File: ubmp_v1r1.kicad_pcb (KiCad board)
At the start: 2 copper layers, 34.5 x 14 mm, 34 parts, among them J1 Conn_02x05_Counter_Clockwise, J2 USB_A, U1 STM32F103CBUx, U2 MIC5245-3.3, Y1 PRQC8.00CR1010V00L

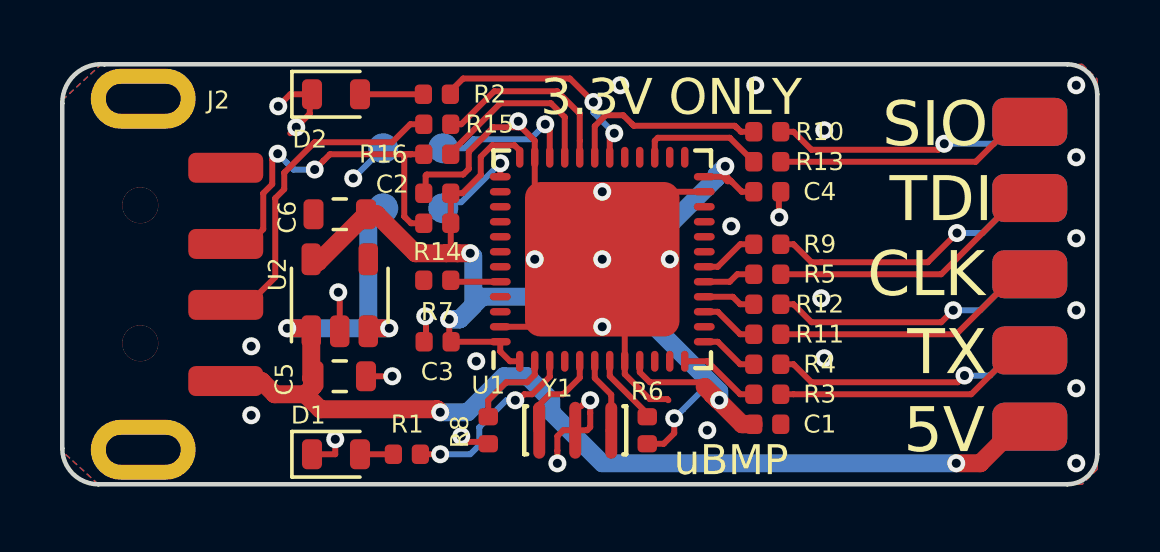
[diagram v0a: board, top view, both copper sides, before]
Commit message: Now more compatible with STLink-v2
Changes:
* Fixed 0603 cap spacing
* Added fuse to 5V line
* Connected unused signals from STLink schematic
* Connected BOOT1 to GND
* Removed yellow LED
* Updated width of USB connector pads for easier soldering
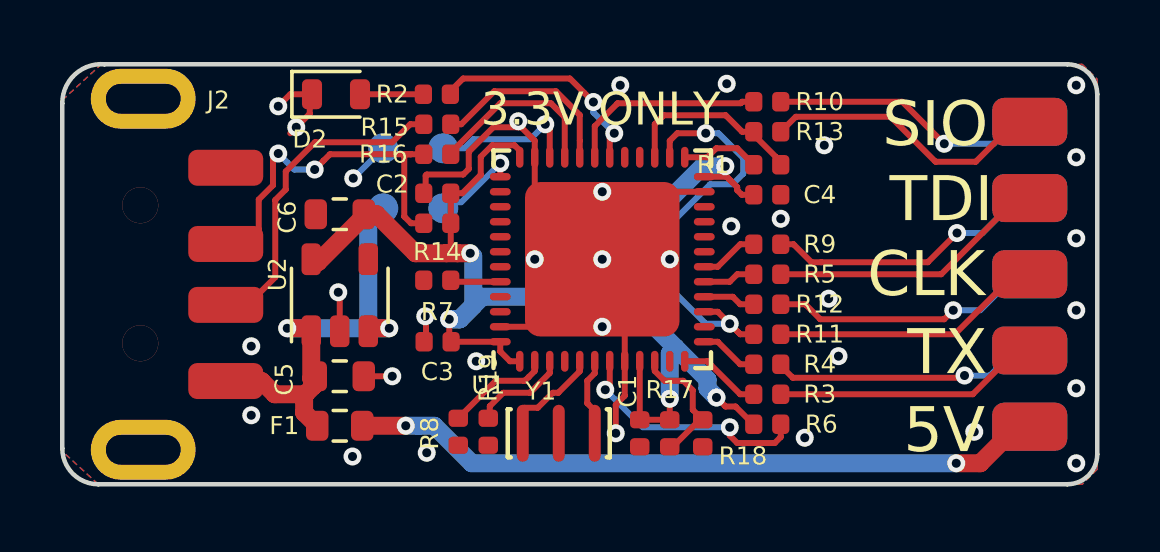
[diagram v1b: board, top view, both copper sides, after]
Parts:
- removed D1: YELLOW, ubmp:D_0603_1608Metric_Rounded
- added F1: MF-FSMF050X-2, ubmp:R_0603_1608Metric_Rounded, F.Cu at (94.2, 111.0)
- added R17: 1.5k, ubmp:R_0402_1005Metric_Rounded, F.Cu at (105.2, 111.3)
- added R18: 1.5k, ubmp:R_0402_1005Metric_Rounded, F.Cu at (106.3, 111.3)
- added R19: 1.5k, ubmp:R_0402_1005Metric_Rounded, F.Cu at (99.2, 111.2)
- R1: value 470 -> 100
- moved R1 15.4 mm to (108.5, 102.3), turned to 0 degrees
- moved C1 4.26 mm to (104.2, 111.3), turned to 270 degrees
- moved R6 4.00 mm to (108.5, 111.0), turned to 180 degrees
- moved R8 1.00 mm to (98.2, 111.2)
- moved R10 1.00 mm to (108.5, 100.2)
- moved R13 1.00 mm to (108.5, 101.2)
- moved Y1 0.56 mm to (101.5, 111.3)
- moved C4 0.10 mm to (108.5, 103.3)
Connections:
- J1 pad 1: +5V -> Net-(F1-Pad1)
- R1 pad 1: /LED_UART -> /STLINK_SWDIO_IN
- R1 pad 2: Net-(D1-Pad2) -> /BMP_SWDIO_TMS
- U1 pad 10: Net-(U1-Pad10) -> /STLINK_AIN_1
- U1 pad 20: Net-(U1-Pad20) -> GND
- U1 pad 25: Net-(U1-Pad25) -> /STLINK_SWDIO_IN
- U1 pad 26: Net-(U1-Pad26) -> /BMP_SWCLK_TCK
- U1 pad 3: /LED_UART -> /STM_ID2
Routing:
- net +5V: track 42.0 -> 16.4 mm, vias 4 -> 2
- net Net-(F1-Pad1): track 0.00 -> 23.3 mm, vias 0 -> 2
- net /BMP_SWCLK_TCK: track 2.02 -> 14.8 mm, vias 0 -> 2
- net /LED_UART: track 6.31 -> 0.00 mm, vias 2 -> 0
- net GND: track 39.3 -> 33.3 mm
- net /NRST: track 2.35 -> 8.27 mm, vias 0 -> 2
- net /STLINK_AIN_1: track 0.00 -> 4.45 mm
- net /STM_ID2: track 0.00 -> 3.35 mm
- net /STLINK_SWDIO_IN: track 0.00 -> 2.65 mm
- net /BMP_SWDIO_TMS: track 4.29 -> 6.22 mm
- net +3V3: track 46.6 -> 45.5 mm
- net Net-(D1-Pad2): track 1.11 -> 0.00 mm
- net /BMP_SWDIO_TMSo: track 8.91 -> 9.68 mm
- net /STM_ID: track 2.96 -> 3.57 mm
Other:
- board text removed: "uBMP"

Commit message: Updated PCB version number, generated new schematic
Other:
- board text added: "µBMP v1.1"
- board text removed: "µBMP v1.0"
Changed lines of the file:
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@@
     (effects (font (size 1.5 1.5) (thickness 0.3)) (justify mirror))
   )
-  (gr_text "µBMP v1.0" (at 101.8 108.6) (layer B.SilkS)
+  (gr_text "µBMP v1.1" (at 101.8 108.6) (layer B.SilkS)
     (effects (font (size 2 2) (thickness 0.4)) (justify mirror))
   )

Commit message: Updated reset circuit and updated silkscreen layout
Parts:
- removed R6: 1.5k, ubmp:R_0402_1005Metric_Rounded
- added C7: 100n, ubmp:C_0402_1005Metric_Rounded, F.Cu at (108.5, 111.0)
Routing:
- net +3V3: track 45.5 -> 41.2 mm, vias 5 -> 4
- net /NRST: track 8.27 -> 6.69 mm

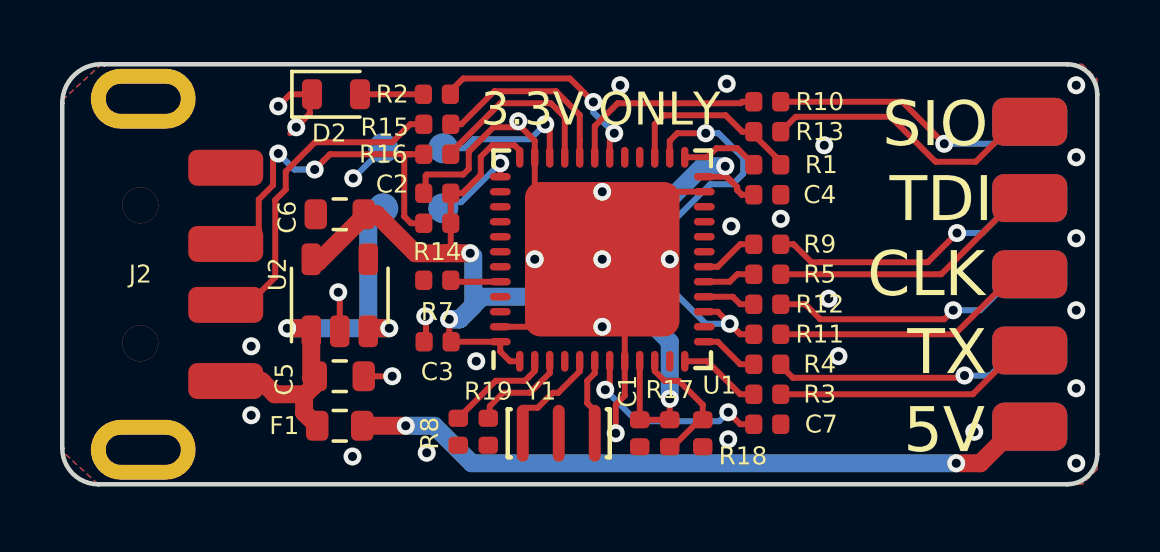
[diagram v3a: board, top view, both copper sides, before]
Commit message: Reverted STlink compatibility changes and updated a lot of footprints
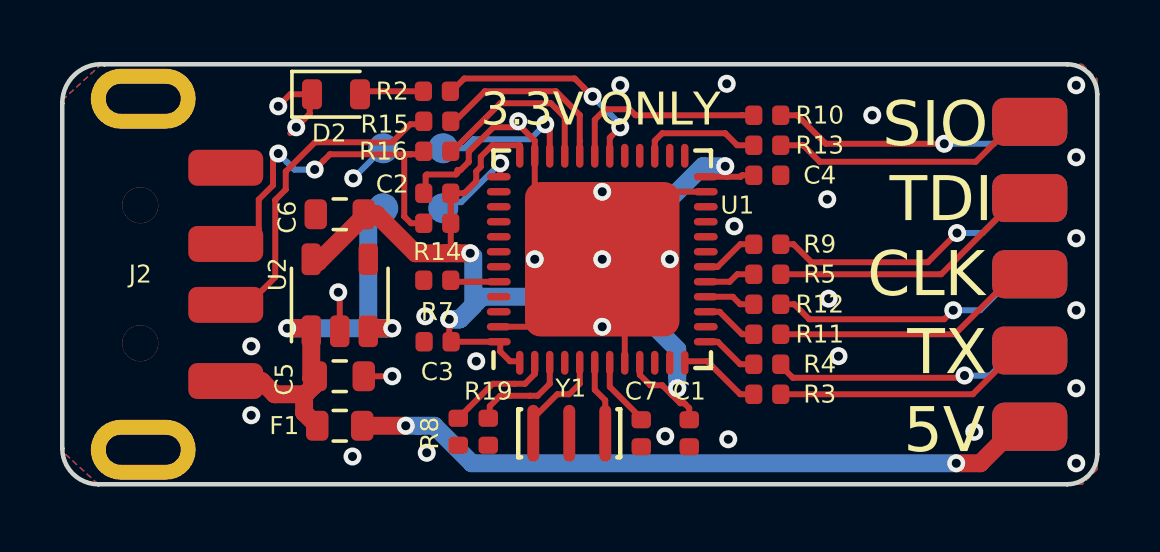
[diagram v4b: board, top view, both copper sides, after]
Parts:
- removed R1: 100, ubmp:R_0402_1005Metric_Rounded
- removed R17, R18: 1.5k, ubmp:R_0402_1005Metric_Rounded
- moved C7 4.21 mm to (104.3, 111.3), turned to 90 degrees
- moved C1 1.65 mm to (105.9, 111.3)
- moved C4 0.65 mm to (108.5, 102.7)
- moved R10 0.45 mm to (108.5, 100.7)
- moved R13 0.45 mm to (108.5, 101.7)
- moved Y1 0.35 mm to (101.9, 111.3)
- moved R15 0.10 mm to (97.5, 100.9)
- moved R16 0.10 mm to (97.5, 101.9)
- moved R2 0.10 mm to (97.5, 99.9)
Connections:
- U1 pad 10: /STLINK_AIN_1 -> Net-(U1-Pad10)
- U1 pad 20: GND -> Net-(U1-Pad20)
- U1 pad 25: /STLINK_SWDIO_IN -> Net-(U1-Pad25)
- U1 pad 26: /BMP_SWCLK_TCK -> Net-(U1-Pad26)
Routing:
- net /BMP_SWCLK_TCK: track 14.8 -> 1.96 mm, vias 2 -> 0
- net /STLINK_AIN_1: track 4.36 -> 0.00 mm
- net /NRST: track 6.69 -> 2.33 mm, vias 2 -> 0
- net GND: track 33.3 -> 29.6 mm
- net /STLINK_SWDIO_IN: track 2.65 -> 0.00 mm
- net /BMP_SWDIO_TMS: track 6.22 -> 4.12 mm
- net +3V3: track 41.2 -> 40.0 mm
- net /BMP_SWDIO_TMSo: track 9.68 -> 9.08 mm
